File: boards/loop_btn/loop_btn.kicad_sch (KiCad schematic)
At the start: 22 parts, among them J6 LOOP, SW1 SW_START, SW2 SW_END, SW3 SW_RELOOP

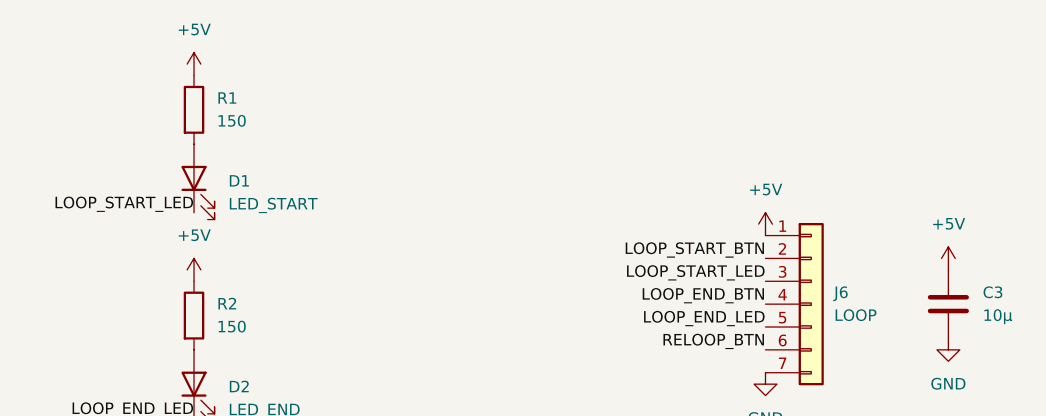
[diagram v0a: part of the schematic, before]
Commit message: boards: loop_btn schematic update; add OneButton V1 STEP model
- loop_btn: schematic revision + project settings.
- midi_s3_mini: project settings.
- one_button: add OneButtonV1.step 3D model.

Co-Authored-By: Claude Opus 4.8 (1M context) <noreply@anthropic.com>
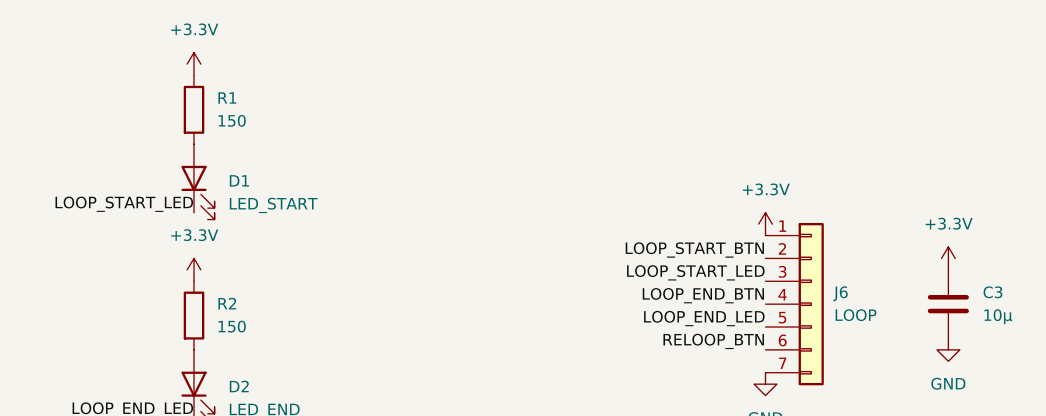
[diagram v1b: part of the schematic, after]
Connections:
- net +5V renamed +3.3V
